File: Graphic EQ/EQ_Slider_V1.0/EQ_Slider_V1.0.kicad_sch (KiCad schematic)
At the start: 23 parts

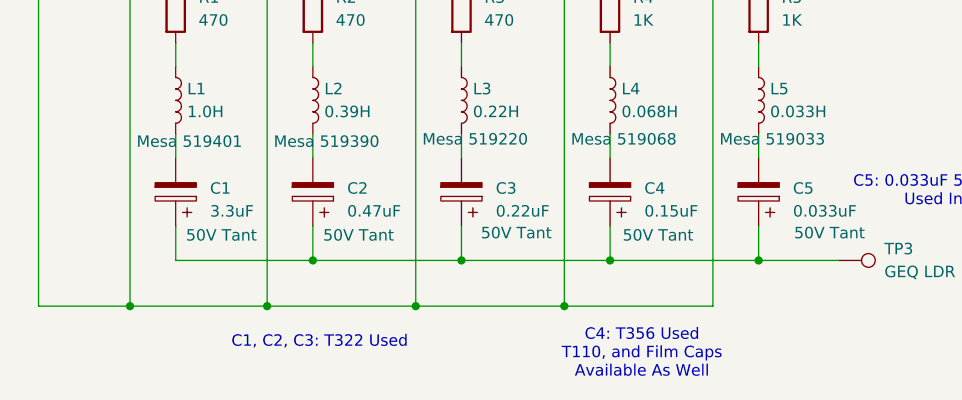
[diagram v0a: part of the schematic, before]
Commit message: Added Comments to EQ Slider PCB
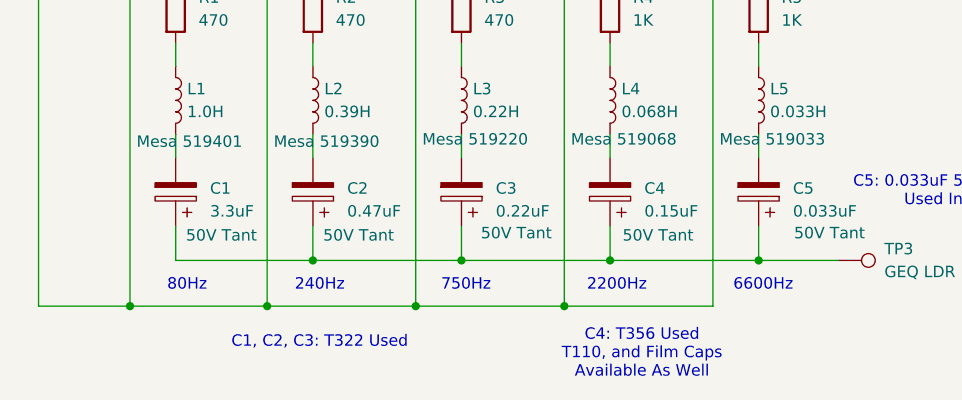
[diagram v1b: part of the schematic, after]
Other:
- note added: "2200Hz"
- note added: "240Hz"
- note added: "6600Hz"
- note added: "750Hz"
- note added: "80Hz"
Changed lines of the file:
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@@
+		)
+	)
+	(text "750Hz"
+		(exclude_from_sim no)
+		(at 131.318 142.494 0)
+		(effects
+			(font
+				(size 1.27 1.27)
+			)
+		)
+	)
+	(text "80Hz"
+		(exclude_from_sim no)
+		(at 100.33 142.494 0)
+		(effects
+			(font
+				(size 1.27 1.27)
+			)
+		)
+	)
+	(text "240Hz"
+		(exclude_from_sim no)
+		(at 115.062 142.494 0)
+		(effects
+			(font
+				(size 1.27 1.27)
+			)
+		)
+	)
+	(text "6600Hz"
+		(exclude_from_sim no)
+		(at 164.338 142.494 0)
+		(effects
+			(font
+				(size 1.27 1.27)
+			)
 		)
 	)
@@
 		(effects
 			(font
+				(size 1.27 1.27)
+			)
+		)
+	)
+	(text "2200Hz"
+		(exclude_from_sim no)
+		(at 148.082 142.494 0)
+		(effects
+			(font
